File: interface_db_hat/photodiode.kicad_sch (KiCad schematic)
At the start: 10 parts, among them J15 Screw_Terminal_01x02, J16 Screw_Terminal_01x02, U10 LM358, U3 BDJ0GA5WEFJ

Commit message: update
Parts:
- removed C47: 100nF, Capacitor_SMD:C_0603_1608Metric_Pad1.08x0.95mm_HandSolder, symbol Device:C
- removed J15, J16: Screw_Terminal_01x02, Terminal_Block_Custom:1x02_P2.54mm_Horizontal, symbol Connector:Screw_Terminal_01x02
- removed U10: LM358, Package_SO:SOIC-8_3.9x4.9mm_P1.27mm, symbol Amplifier_Operational:LM358
- removed U3: BDJ0GA5WEFJ, Package_SO:HTSOP-8-1EP_3.9x4.9mm_P1.27mm_EP2.4x3.2mm, symbol Regulator_Linear:BDJ0GA5WEFJ
- added C51, C52: 100nF, Capacitor_SMD:C_0603_1608Metric_Pad1.08x0.95mm_HandSolder, symbol Device:C
- added J7: USB_B_Mini, symbol Connector:USB_B_Mini
- added JP9: SolderJumper_2_Open, Jumper:SolderJumper-2_P1.3mm_Open_TrianglePad1.0x1.5mm, symbol Jumper:SolderJumper_2_Open
- added R20: 50, Resistor_SMD:R_0603_1608Metric_Pad0.98x0.95mm_HandSolder, symbol Device:R_US
- added R21: 10k, Resistor_SMD:R_0603_1608Metric_Pad0.98x0.95mm_HandSolder, symbol Device:R_US
- added R22, R23: 0, Resistor_SMD:R_0603_1608Metric_Pad0.98x0.95mm_HandSolder, symbol Device:R_US
- added U3: ADS1115IDGS, Package_SO:TSSOP-10_3x3mm_P0.5mm, symbol Analog_ADC:ADS1115IDGS
- added U4, U5: OPA320AIDBVR, DBV5, symbol OPA320:OPA320AIDBVR
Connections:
- net +12V is gone; now on net GND: C50.2
- net GND: now also C51.2, C52.2, J7.2 (D-), J7.4 (ID), J7.5 (GND), J7.SH (Shield), R20.1, U3.3 (GND), U4.2 (V-), U4.3 (IN+), U5.2 (V-), U5.3 (IN+); no longer C50.1
- net PD_OUT1: now also R22.1, U3.4 (AIN0); no longer C48.1, R18.2
- net PD_OUT2: now also R23.1, U3.5 (AIN1); no longer C49.1, R19.2
- net at C49.2, R19.1: now also U5.4 (IN-)
- net at C48.2, R18.1: now also U4.4 (IN-)
- new net: C48.1, R18.2, R22.2, U4.1 (OUT)
- new net: C49.1, R19.2, R23.2, U5.1 (OUT)
- new net: JP9.1 (A), R20.2, U3.1 (ADDR)
- new net: R21.2, U3.2 (ALERT/RDY)
- new net +5V: C50.1, C51.1, C52.1, JP9.2 (B), R21.1, U3.8 (VDD), U4.5 (V+), U5.5 (V+)
- new net I2C_SCL: U3.10 (SCL)
- new net I2C_SDA: U3.9 (SDA)
- new net PD1_ANODE: J7.1 (VBUS)
- new net PD2_ANODE: J7.3 (D+)
- no-connect marks 0 -> 2
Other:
- moved on the sheet: C48, C49, R18, R19

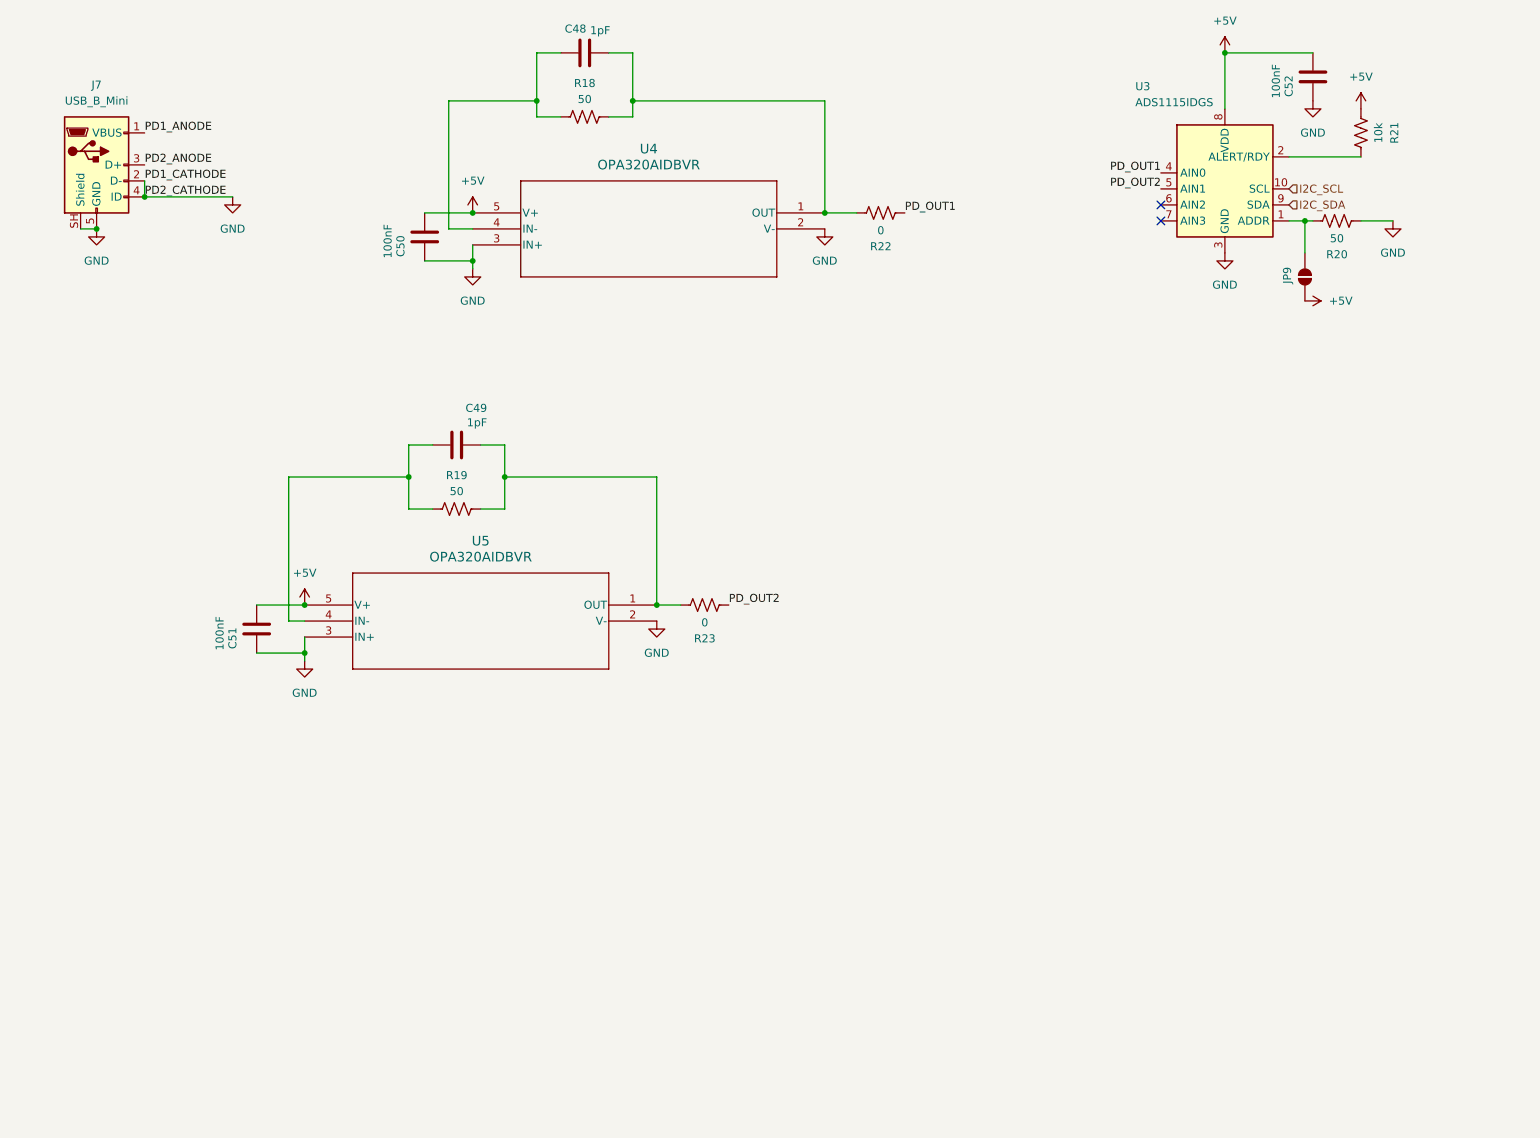
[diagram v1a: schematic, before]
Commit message: starting interface layout
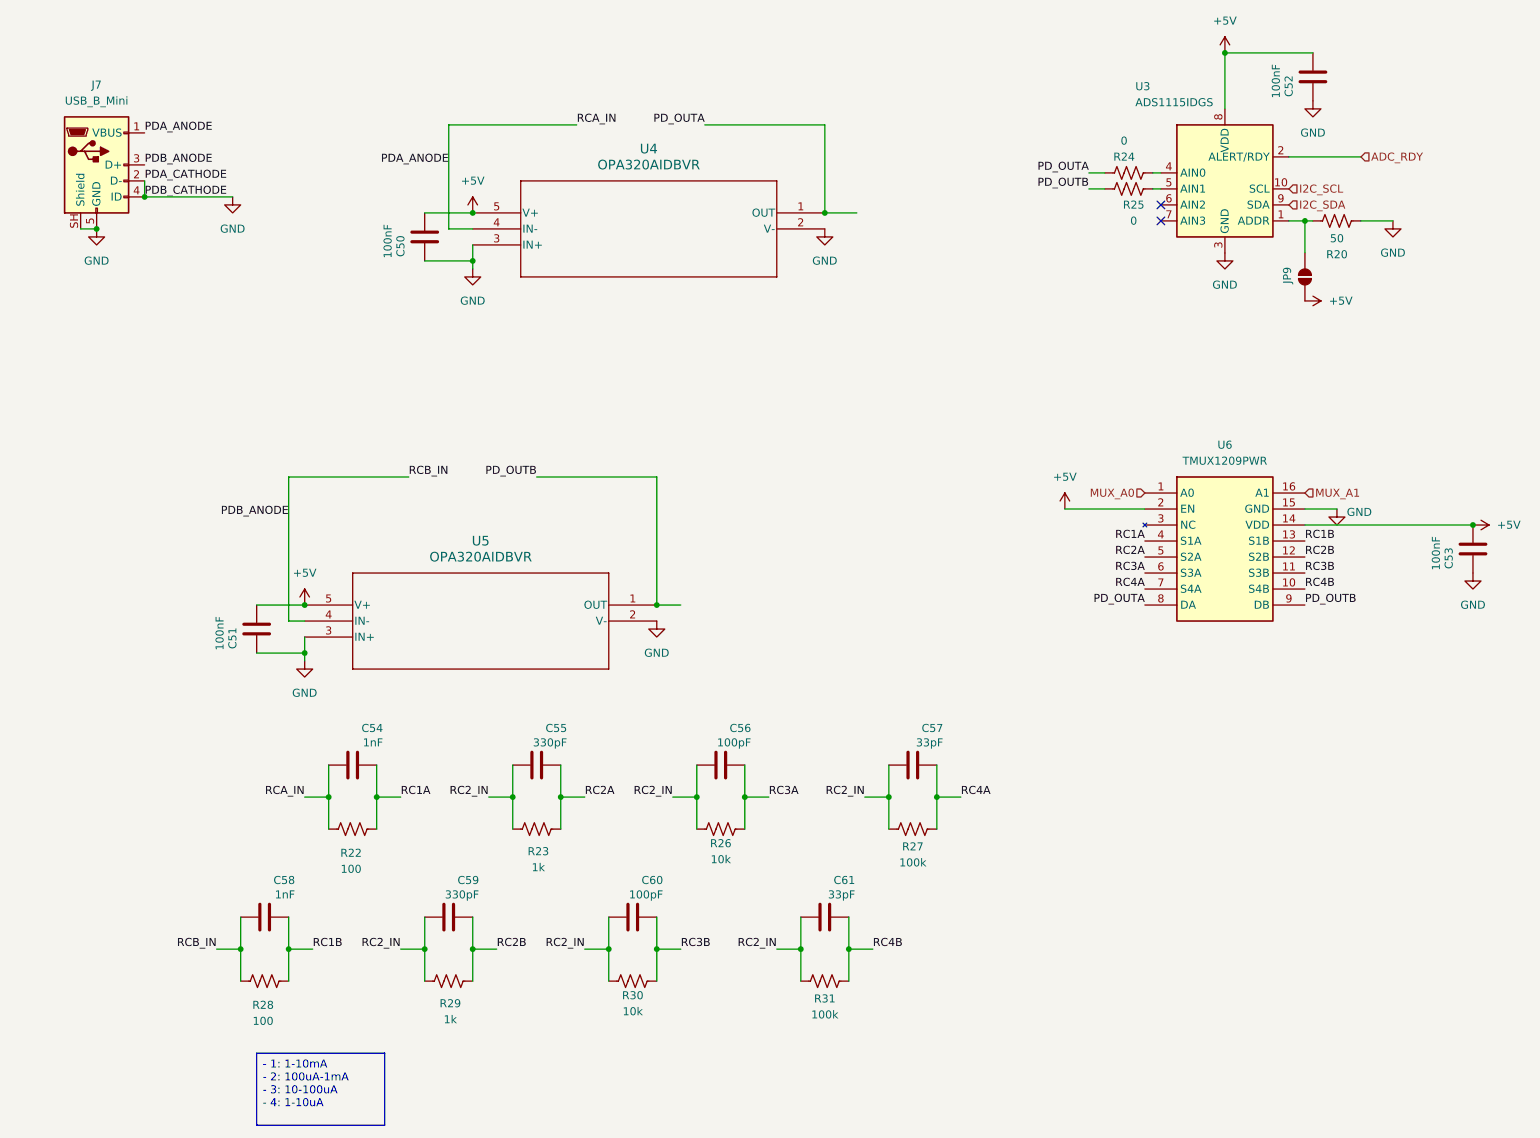
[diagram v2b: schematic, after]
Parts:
- removed C48, C49: 1pF, Capacitor_SMD:C_0603_1608Metric_Pad1.08x0.95mm_HandSolder, symbol Device:C
- removed R18, R19: 50, Resistor_SMD:R_0603_1608Metric_Pad0.98x0.95mm_HandSolder, symbol Device:R_US
- removed R21: 10k, Resistor_SMD:R_0603_1608Metric_Pad0.98x0.95mm_HandSolder, symbol Device:R_US
- added C53: 100nF, Capacitor_SMD:C_0603_1608Metric_Pad1.08x0.95mm_HandSolder, symbol Device:C
- added C54, C58: 1nF, Capacitor_SMD:C_0603_1608Metric_Pad1.08x0.95mm_HandSolder, symbol Device:C
- added C55, C59: 330pF, Capacitor_SMD:C_0603_1608Metric_Pad1.08x0.95mm_HandSolder, symbol Device:C
- added C56, C60: 100pF, Capacitor_SMD:C_0603_1608Metric_Pad1.08x0.95mm_HandSolder, symbol Device:C
- added C57, C61: 33pF, Capacitor_SMD:C_0603_1608Metric_Pad1.08x0.95mm_HandSolder, symbol Device:C
- added R24, R25: 0, Resistor_SMD:R_0603_1608Metric_Pad0.98x0.95mm_HandSolder, symbol Device:R_US
- added R26, R30: 10k, Resistor_SMD:R_0603_1608Metric_Pad0.98x0.95mm_HandSolder, symbol Device:R_US
- added R27, R31: 100k, Resistor_SMD:R_0603_1608Metric_Pad0.98x0.95mm_HandSolder, symbol Device:R_US
- added R28: 100, Resistor_SMD:R_0603_1608Metric_Pad0.98x0.95mm_HandSolder, symbol Device:R_US
- added R29: 1k, Resistor_SMD:R_0603_1608Metric_Pad0.98x0.95mm_HandSolder, symbol Device:R_US
- added U6: TMUX1209PWR, Package_SO:TSSOP-16_4.4x5mm_P0.65mm, symbol TMUX1209:TMUX1209PWR
- J7: footprint (none) -> Connector_USB:USB_Mini-B_Wuerth_65100516121_Horizontal
- R22: value 0 -> 100
- R23: value 0 -> 1k
- U4, U5: footprint DBV5 -> OPA320:DBV5
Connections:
- net PD1_ANODE is gone; now on net PDA_ANODE: J7.1 (VBUS)
- net PD2_ANODE is gone; now on net PDB_ANODE: J7.3 (D+)
- net +5V: now also C53.1, U6.14 (VDD), U6.2 (EN)
- net GND: now also C53.2, U6.15 (GND)
- net PD_OUTA: now reaches U4.1 (OUT)
- net PD_OUTA: now also R24.2, U6.8 (DA); no longer R22.2
- net PD_OUTB: now reaches U5.1 (OUT)
- net PD_OUTB: now also R25.1, U6.9 (DB); no longer R23.2
- net PDB_ANODE: now reaches U5.4 (IN-)
- net PDB_ANODE: now also C58.2, R28.1
- net PDA_ANODE: now reaches U4.4 (IN-)
- net PDA_ANODE: now also R22.1, C54.2
- net ADC_RDY: now reaches U3.2 (ALERT/RDY)
- net PD_OUT1: no longer names the net of U3.4 (AIN0)
- net PD_OUT1: now also R24.1; no longer R22.1
- net PD_OUT2: no longer names the net of U3.5 (AIN1)
- net PD_OUT2: now also R25.2; no longer R23.1
- new net MUX_A0: U6.1 (A0)
- new net MUX_A1: U6.16 (A1)
- new net RC1A: C54.1, R22.2, U6.4 (S1A)
- new net RC1B: C58.1, R28.2, U6.13 (S1B)
- new net RC2A: C55.1, R23.2, U6.5 (S2A)
- new net RC2B: C59.1, R29.2, U6.12 (S2B)
- new net RC2_IN: C55.2, C56.2, C57.2, C59.2, C60.2, C61.2, R23.1, R26.1, R27.1, R29.1, R30.1, R31.1
- new net RC3A: C56.1, R26.2, U6.6 (S3A)
- new net RC3B: C60.1, R30.2, U6.11 (S3B)
- new net RC4A: C57.1, R27.2, U6.7 (S4A)
- new net RC4B: C61.1, R31.2, U6.10 (S4B)

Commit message: interface layout done
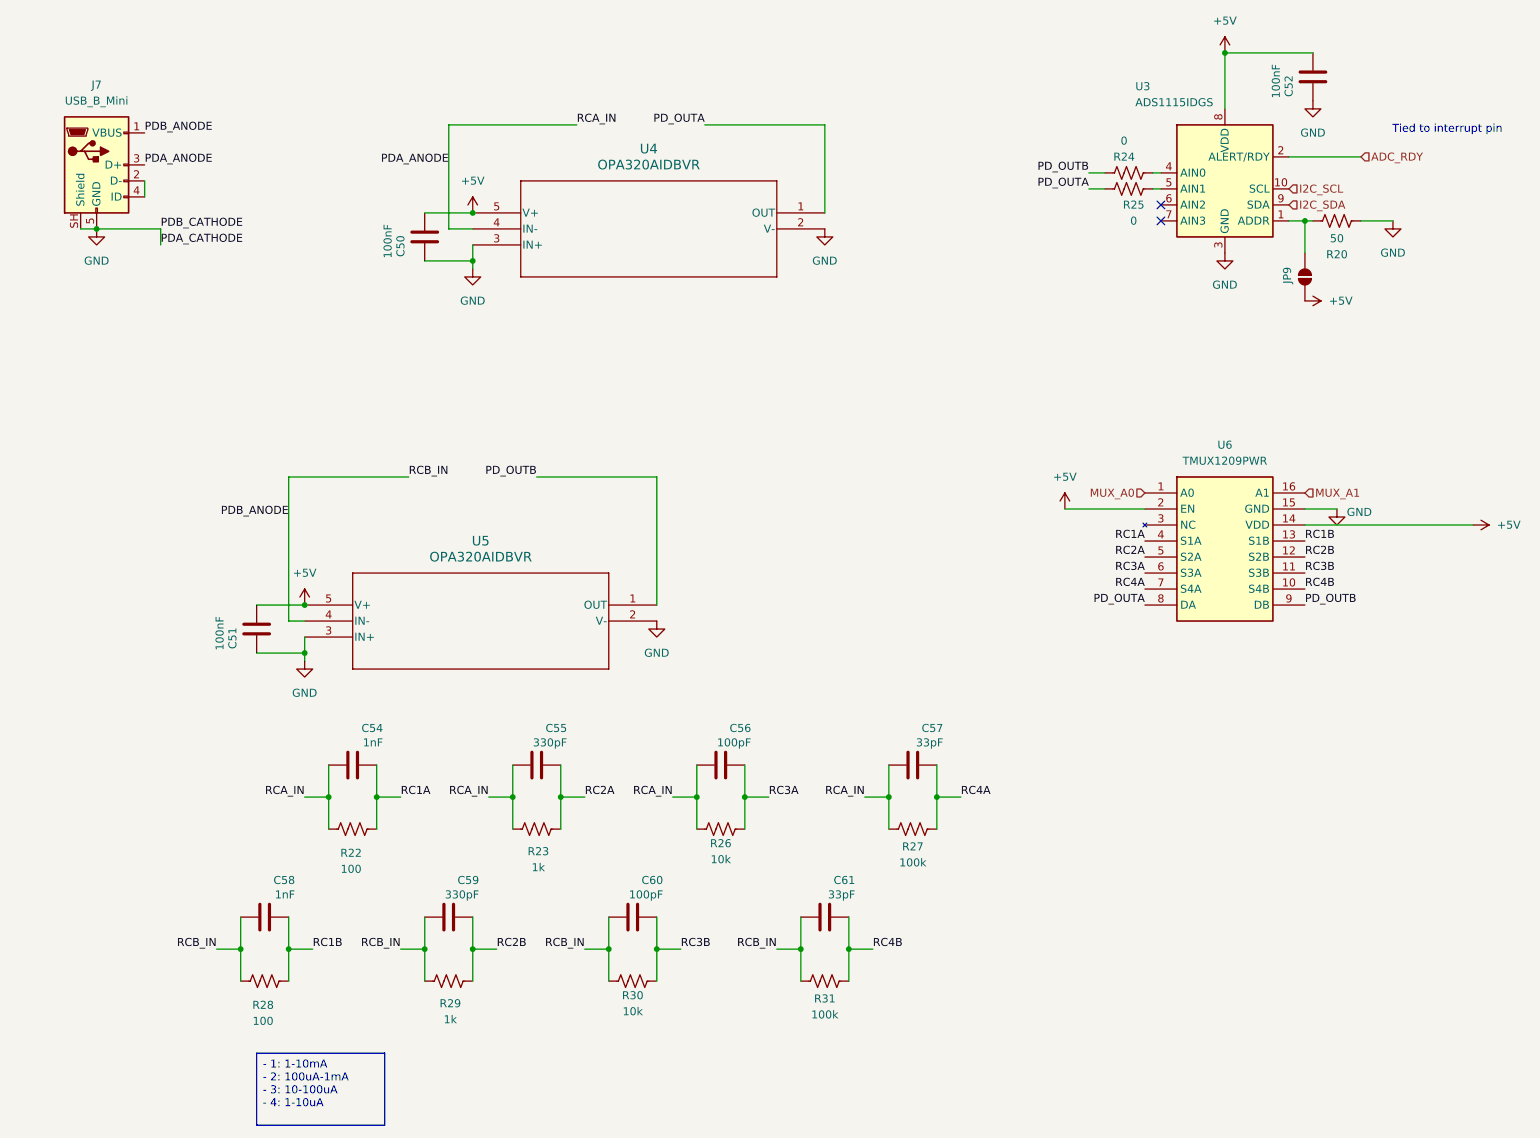
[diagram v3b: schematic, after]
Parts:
- removed C53: 100nF, Capacitor_SMD:C_0603_1608Metric_Pad1.08x0.95mm_HandSolder, symbol Device:C
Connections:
- net GND: no longer J7.2 (D-), J7.4 (ID)
- net PDA_ANODE: now also C55.2, C56.2, C57.2, J7.3 (D+), R23.1, R26.1, R27.1; no longer J7.1 (VBUS)
- net PDB_ANODE: now also C59.2, C60.2, C61.2, J7.1 (VBUS), R29.1, R30.1, R31.1; no longer J7.3 (D+)
- net PD_OUTA: now also R25.1; no longer R24.2
- net PD_OUTB: now also R24.2; no longer R25.1
- removed net RC2_IN: C55.2, C56.2, C57.2, C59.2, C60.2, C61.2, R23.1, R26.1, R27.1, R29.1, R30.1, R31.1
- new net: J7.2 (D-), J7.4 (ID)
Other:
- note added: "Tied to interrupt pin"

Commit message: fixed interface schematic
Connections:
- net GND: now also J7.2 (D-), J7.4 (ID)
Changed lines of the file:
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@@
+	)
+	(junction
+		(at 39.37 48.26)
+		(diameter 0)
+		(color 0 0 0 0)
 	)
 	(junction
 		(at 31.75 53.34)
+		(diameter 0)
+		(color 0 0 0 0)
+	)
+	(junction
+		(at 39.37 53.34)
 		(diameter 0)
 		(color 0 0 0 0)
@@
 	(wire
 		(pts
-			(xy 31.75 53.34) (xy 41.91 53.34)
+			(xy 31.75 53.34) (xy 39.37 53.34)
 		)
 		(stroke
@@
 	(wire
 		(pts
+			(xy 39.37 48.26) (xy 39.37 53.34)
+		)
+		(stroke
+			(width 0)
+			(type default)
+		)
+	)
+	(wire
+		(pts
 			(xy 54.61 162.56) (xy 54.61 167.64)
 		)
@@
 		)
 		(stroke
+			(width 0)
+			(type default)
+		)
+	)
+	(wire
+		(pts
+			(xy 39.37 53.34) (xy 41.91 53.34)
+		)
+		(stroke

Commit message: update
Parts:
- added C?: 100nF, Capacitor_SMD:C_0603_1608Metric, symbol Device:C
- added R9: 10k, Resistor_SMD:R_0603_1608Metric, symbol Device:R_US
- added TH1: NCU18XH103F60RB, Resistor_SMD:R_0603_1608Metric, symbol Device:Thermistor_US
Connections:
- net GND: now also C?.2, TH1.2; no longer J7.2 (D-), J7.4 (ID)
- net PDA_ANODE: now also J7.2 (D-); no longer J7.3 (D+)
- new net +3V3: R9.2
- new net NTC: C?.1, R9.1, TH1.1
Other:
- note added: "Thermistor"
- moved on the sheet: J7

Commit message: jlc order
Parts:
- removed C50, C51, C52: 100nF, Capacitor_SMD:C_0603_1608Metric_Pad1.08x0.95mm_HandSolder, symbol Device:C
- removed C54, C58: 1nF, Capacitor_SMD:C_0603_1608Metric_Pad1.08x0.95mm_HandSolder, symbol Device:C
- removed C55, C59: 330pF, Capacitor_SMD:C_0603_1608Metric_Pad1.08x0.95mm_HandSolder, symbol Device:C
- removed C56, C60: 100pF, Capacitor_SMD:C_0603_1608Metric_Pad1.08x0.95mm_HandSolder, symbol Device:C
- removed C57, C61: 33pF, Capacitor_SMD:C_0603_1608Metric_Pad1.08x0.95mm_HandSolder, symbol Device:C
- removed C?: 100nF, Capacitor_SMD:C_0603_1608Metric, symbol Device:C
- removed J7: USB_B_Mini, Connector_USB:USB_Mini-B_Wuerth_65100516121_Horizontal, symbol Connector:USB_B_Mini
- removed JP9: SolderJumper_2_Open, Jumper:SolderJumper-2_P1.3mm_Open_TrianglePad1.0x1.5mm, symbol Jumper:SolderJumper_2_Open
- removed R20: 50, Resistor_SMD:R_0603_1608Metric_Pad0.98x0.95mm_HandSolder, symbol Device:R_US
- removed R22, R28: 100, Resistor_SMD:R_0603_1608Metric_Pad0.98x0.95mm_HandSolder, symbol Device:R_US
- removed R23, R29: 1k, Resistor_SMD:R_0603_1608Metric_Pad0.98x0.95mm_HandSolder, symbol Device:R_US
- removed R24, R25: 0, Resistor_SMD:R_0603_1608Metric_Pad0.98x0.95mm_HandSolder, symbol Device:R_US
- removed R26, R30: 10k, Resistor_SMD:R_0603_1608Metric_Pad0.98x0.95mm_HandSolder, symbol Device:R_US
- removed R27, R31: 100k, Resistor_SMD:R_0603_1608Metric_Pad0.98x0.95mm_HandSolder, symbol Device:R_US
- removed R9: 10k, Resistor_SMD:R_0603_1608Metric, symbol Device:R_US
- removed TH1: NCU18XH103F60RB, Resistor_SMD:R_0603_1608Metric, symbol Device:Thermistor_US
- removed U3: ADS1115IDGS, Package_SO:TSSOP-10_3x3mm_P0.5mm, symbol Analog_ADC:ADS1115IDGS
- removed U4, U5: OPA320AIDBVR, OPA320:DBV5, symbol OPA320:OPA320AIDBVR
- removed U6: TMUX1209PWR, Package_SO:TSSOP-16_4.4x5mm_P0.65mm, symbol TMUX1209:TMUX1209PWR
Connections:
- no-connect marks 2 -> 0
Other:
- note removed: "Thermistor"
- note removed: "Tied to interrupt pin"
